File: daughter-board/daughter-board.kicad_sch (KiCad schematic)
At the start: 8 parts, among them J1 USB-C Connector, J2 Ribbon Connector, P1 IPOD_CONNECTOR_MALE, U1 AP2331SA-7

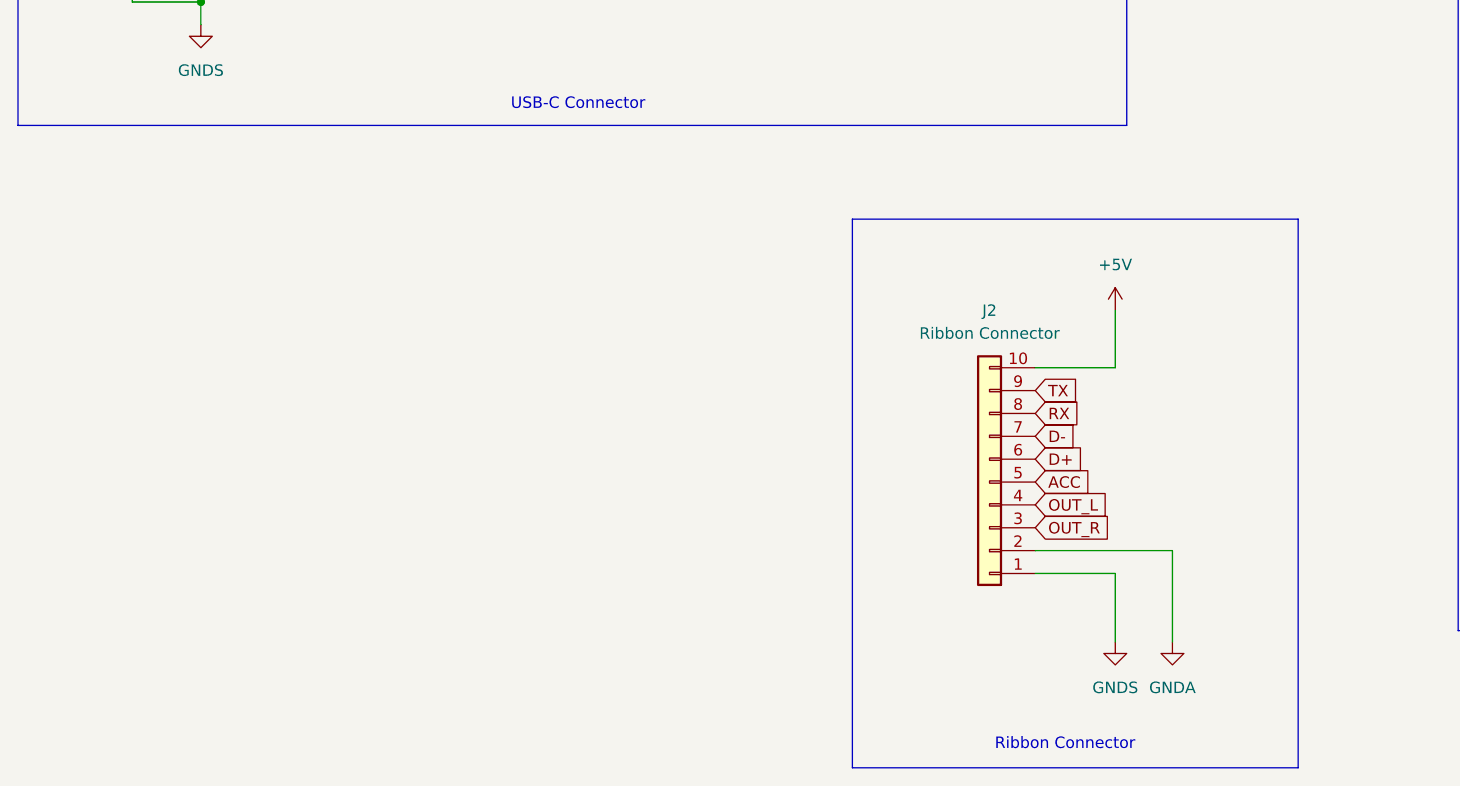
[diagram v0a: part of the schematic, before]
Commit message: Change FFC to match fab house.
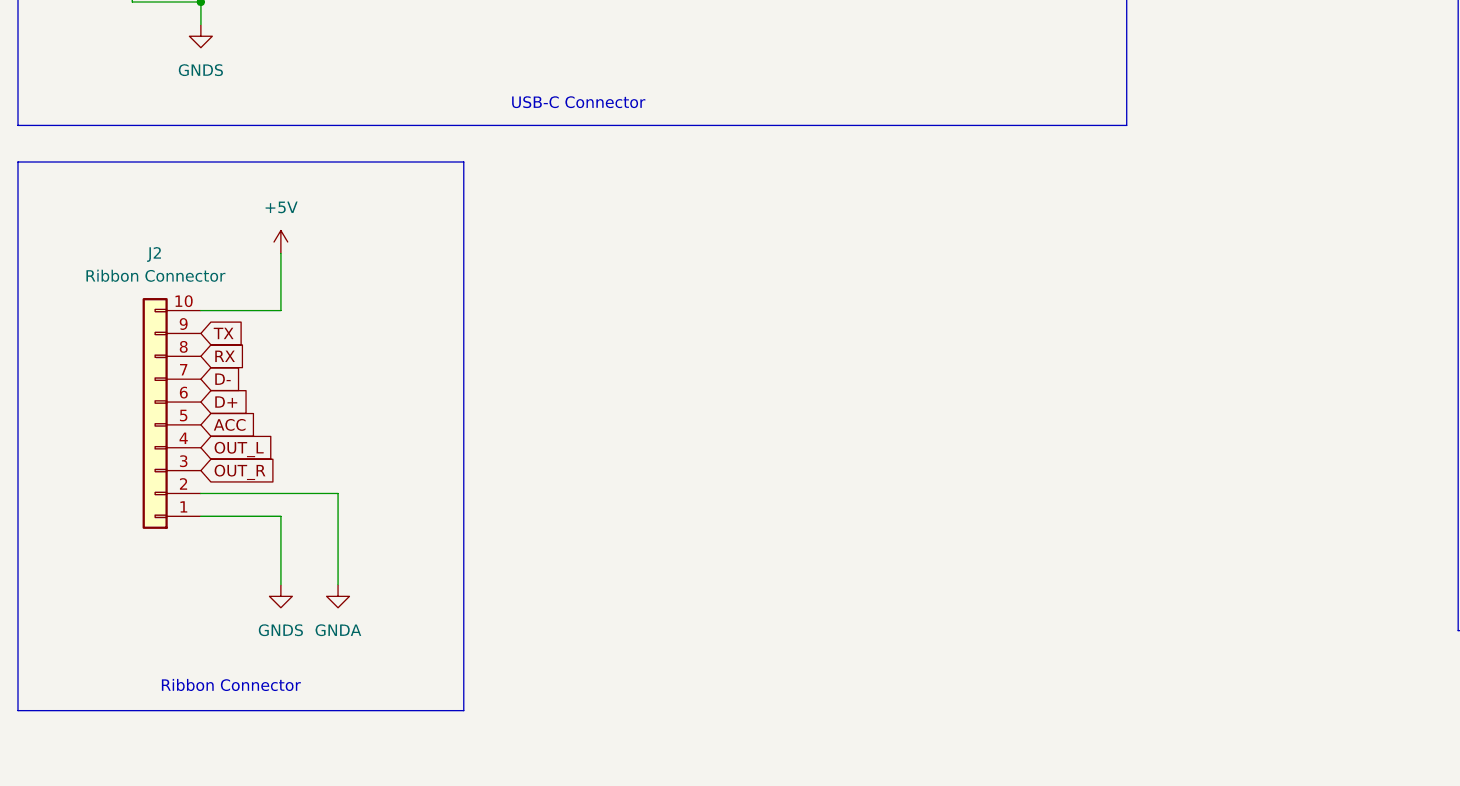
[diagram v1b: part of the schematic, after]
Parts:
- C1, C2: footprint (none) -> Capacitor_SMD:C_0805_2012Metric_Pad1.18x1.45mm_HandSolder
- J2: footprint (none) -> Connector_FFC-FPC:Molex_54548-1071_1x10-1MP_P0.5mm_Horizontal
- U1: footprint AP2331SA-7:SOT91P240X120-3N -> AP2331SA:SOT91P240X120-3N
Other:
- moved on the sheet: J2
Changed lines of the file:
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@@
 	(paper "A4")
 	(rectangle
-		(start 114.3 100.33)
-		(end 163.83 161.29)
+		(start 21.59 93.98)
+		(end 71.12 154.94)
 		(stroke
 			(width 0)
@@
 	(text "Ribbon Connector"
 		(exclude_from_sim no)
-		(at 137.922 158.75 0)
+		(at 45.212 152.4 0)
 		(effects
 			(font
@@
 	(wire
 		(pts
-			(xy 134.62 116.84) (xy 143.51 116.84)
-		)
-		(stroke
-			(width 0)
-			(type default)
-		)
-	)
-	(wire
-		(pts
-			(xy 143.51 139.7) (xy 143.51 147.32)
+			(xy 41.91 110.49) (xy 50.8 110.49)
+		)
+		(stroke
+			(width 0)
+			(type default)
+		)
+	)
+	(wire
+		(pts
+			(xy 50.8 133.35) (xy 50.8 140.97)
 		)
 		(stroke
@@
 	(wire
 		(pts
-			(xy 134.62 139.7) (xy 143.51 139.7)
+			(xy 41.91 133.35) (xy 50.8 133.35)
 		)
 		(stroke
@@
 	(wire
 		(pts
-			(xy 143.51 116.84) (xy 143.51 110.49)
+			(xy 50.8 110.49) (xy 50.8 104.14)
 		)
 		(stroke
@@
 	(wire
 		(pts
-			(xy 149.86 137.16) (xy 149.86 147.32)
+			(xy 57.15 130.81) (xy 57.15 140.97)
 		)
 		(stroke
@@
 	(wire
 		(pts
-			(xy 134.62 137.16) (xy 149.86 137.16)
+			(xy 41.91 130.81) (xy 57.15 130.81)
 		)
 		(stroke
@@
 	(global_label "ACC"
 		(shape input)
-		(at 134.62 129.54 0)
+		(at 41.91 123.19 0)
 		(fields_autoplaced yes)
 		(effects
@@
 		)
 		(property "Intersheetrefs" "${INTERSHEET_REFS}"
-			(at 141.2338 129.54 0)
+			(at 48.5238 123.19 0)
 			(effects
 				(font
@@
 	(global_label "D+"
 		(shape input)
-		(at 134.62 127 0)
+		(at 41.91 120.65 0)
 		(fields_autoplaced yes)
 		(effects
@@
 		)
 		(property "Intersheetrefs" "${INTERSHEET_REFS}"
-			(at 140.4476 127 0)
+			(at 47.7376 120.65 0)
 			(effects
 				(font
@@
 	(global_label "TX"
 		(shape input)
-		(at 134.62 119.38 0)
+		(at 41.91 113.03 0)
 		(fields_autoplaced yes)
 		(effects
@@
 		)
 		(property "Intersheetrefs" "${INTERSHEET_REFS}"
-			(at 139.7823 119.38 0)
+			(at 47.0723 113.03 0)
 			(effects
 				(font
@@
 	(global_label "D-"
 		(shape input)
-		(at 134.62 124.46 0)
+		(at 41.91 118.11 0)
 		(fields_autoplaced yes)
 		(effects
@@
 		)
 		(property "Intersheetrefs" "${INTERSHEET_REFS}"
-			(at 140.4476 124.46 0)
+			(at 47.7376 118.11 0)
 			(effects
 				(font
@@
 	(global_label "RX"
 		(shape input)
-		(at 134.62 121.92 0)
+		(at 41.91 115.57 0)
 		(fields_autoplaced yes)
 		(effects
@@
 		)
 		(property "Intersheetrefs" "${INTERSHEET_REFS}"
-			(at 140.0847 121.92 0)
+			(at 47.3747 115.57 0)
 			(effects
 				(font
@@
 	(global_label "OUT_L"
 		(shape input)
-		(at 134.62 132.08 0)
+		(at 41.91 125.73 0)
 		(fields_autoplaced yes)
 		(effects
@@
 		)
 		(property "Intersheetrefs" "${INTERSHEET_REFS}"
-			(at 143.2295 132.08 0)
+			(at 50.5195 125.73 0)
 			(effects
 				(font
@@
 	(global_label "OUT_R"
 		(shape input)
-		(at 134.62 134.62 0)
+		(at 41.91 128.27 0)
 		(fields_autoplaced yes)
 		(effects
@@
 		)
 		(property "Intersheetrefs" "${INTERSHEET_REFS}"
-			(at 143.4714 134.62 0)
+			(at 50.7614 128.27 0)
 			(effects
 				(font
@@
 			)
 		)
-		(property "Footprint" "AP2331SA-7:SOT91P240X120-3N"
+		(property "Footprint" "AP2331SA:SOT91P240X120-3N"
 			(at 107.95 38.1 0)
 			(effects
@@
 	(symbol
 		(lib_id "power:+5V")
-		(at 143.51 110.49 0)
+		(at 50.8 104.14 0)
 		(unit 1)
 		(exclude_from_sim no)
@@
 		(fields_autoplaced yes)
 		(property "Reference" "#PWR01"
-			(at 143.51 114.3 0)
+			(at 50.8 107.95 0)
 			(effects
 				(font
@@
 		)
 		(property "Value" "+5V"
-			(at 143.51 105.41 0)
+			(at 50.8 99.06 0)
 			(effects
 				(font
@@
 		)
 		(property "Footprint" ""
-			(at 143.51 110.49 0)
+			(at 50.8 104.14 0)
 			(effects
 				(font
@@
 		)
 		(property "Datasheet" ""
-			(at 143.51 110.49 0)
+			(at 50.8 104.14 0)
 			(effects
 				(font
@@
 		)
 		(property "Description" "Power symbol creates a global label with name \"+5V\""
-			(at 143.51 110.49 0)
+			(at 50.8 104.14 0)
 			(effects
 				(font
@@
 	(symbol
 		(lib_id "power:GNDA")
-		(at 149.86 147.32 0)
+		(at 57.15 140.97 0)
 		(unit 1)
 		(exclude_from_sim no)
@@
 		(fields_autoplaced yes)
 		(property "Reference" "#PWR011"
-			(at 149.86 153.67 0)
+			(at 57.15 147.32 0)
 			(effects
 				(font
@@
 		)
 		(property "Value" "GNDA"
-			(at 149.86 152.4 0)
+			(at 57.15 146.05 0)
 			(effects
 				(font
@@
 		)
 		(property "Footprint" ""
-			(at 149.86 147.32 0)
+			(at 57.15 140.97 0)
 			(effects
 				(font
@@
 		)
 		(property "Datasheet" ""
-			(at 149.86 147.32 0)
+			(at 57.15 140.97 0)
 			(effects
 				(font
@@
 		)
 		(property "Description" "Power symbol creates a global label with name \"GNDA\" , analog ground"
-			(at 149.86 147.32 0)
+			(at 57.15 140.97 0)
 			(effects
 				(font
@@
 			)
 		)
-		(property "Footprint" ""
+		(property "Footprint" "Capacitor_SMD:C_0805_2012Metric_Pad1.18x1.45mm_HandSolder"
 			(at 129.2352 43.18 0)
 			(effects
@@
 	(symbol
 		(lib_id "Connector_Generic:Conn_01x10")
-		(at 129.54 129.54 180)
+		(at 36.83 123.19 180)
 		(unit 1)
 		(exclude_from_sim no)
@@
 		(fields_autoplaced yes)
 		(property "Reference" "J2"
-			(at 129.54 110.49 0)
+			(at 36.83 104.14 0)
 			(effects
 				(font
@@
 		)
 		(property "Value" "Ribbon Connector"
-			(at 129.54 113.03 0)
-			(effects
-				(font
-					(size 1.27 1.27)
-				)
-			)
-		)
-		(property "Footprint" ""
-			(at 129.54 129.54 0)
+			(at 36.83 106.68 0)
+			(effects
+				(font
+					(size 1.27 1.27)
+				)
+			)
+		)
+		(property "Footprint" "Connector_FFC-FPC:Molex_54548-1071_1x10-1MP_P0.5mm_Horizontal"
+			(at 36.83 123.19 0)
 			(effects
 				(font
@@
 		)
 		(property "Datasheet" "~"
-			(at 129.54 129.54 0)
+			(at 36.83 123.19 0)
 			(effects
 				(font
@@
 		)
 		(property "Description" "Generic connector, single row, 01x10, script generated (kicad-library-utils/schlib/autogen/connector/)"
-			(at 129.54 129.54 0)
+			(at 36.83 123.19 0)
 			(effects
 				(font
@@
 	(symbol
 		(lib_id "power:GNDS")
-		(at 143.51 147.32 0)
+		(at 50.8 140.97 0)
 		(unit 1)
 		(exclude_from_sim no)
@@
 		(fields_autoplaced yes)
 		(property "Reference" "#PWR05"
-			(at 143.51 153.67 0)
+			(at 50.8 147.32 0)
 			(effects
 				(font
@@
 		)
 		(property "Value" "GNDS"
-			(at 143.51 152.4 0)
+			(at 50.8 146.05 0)
 			(effects
 				(font
@@
 		)
 		(property "Footprint" ""
-			(at 143.51 147.32 0)
+			(at 50.8 140.97 0)
 			(effects
 				(font
@@
 		)
 		(property "Datasheet" ""
-			(at 143.51 147.32 0)
+			(at 50.8 140.97 0)
 			(effects
 				(font
@@
 		)
 		(property "Description" "Power symbol creates a global label with name \"GNDS\" , signal ground"
-			(at 143.51 147.32 0)
+			(at 50.8 140.97 0)
 			(effects
 				(font
@@
 			)
 		)
-		(property "Footprint" ""
+		(property "Footprint" "Capacitor_SMD:C_0805_2012Metric_Pad1.18x1.45mm_HandSolder"
 			(at 89.8652 43.18 0)
 			(effects

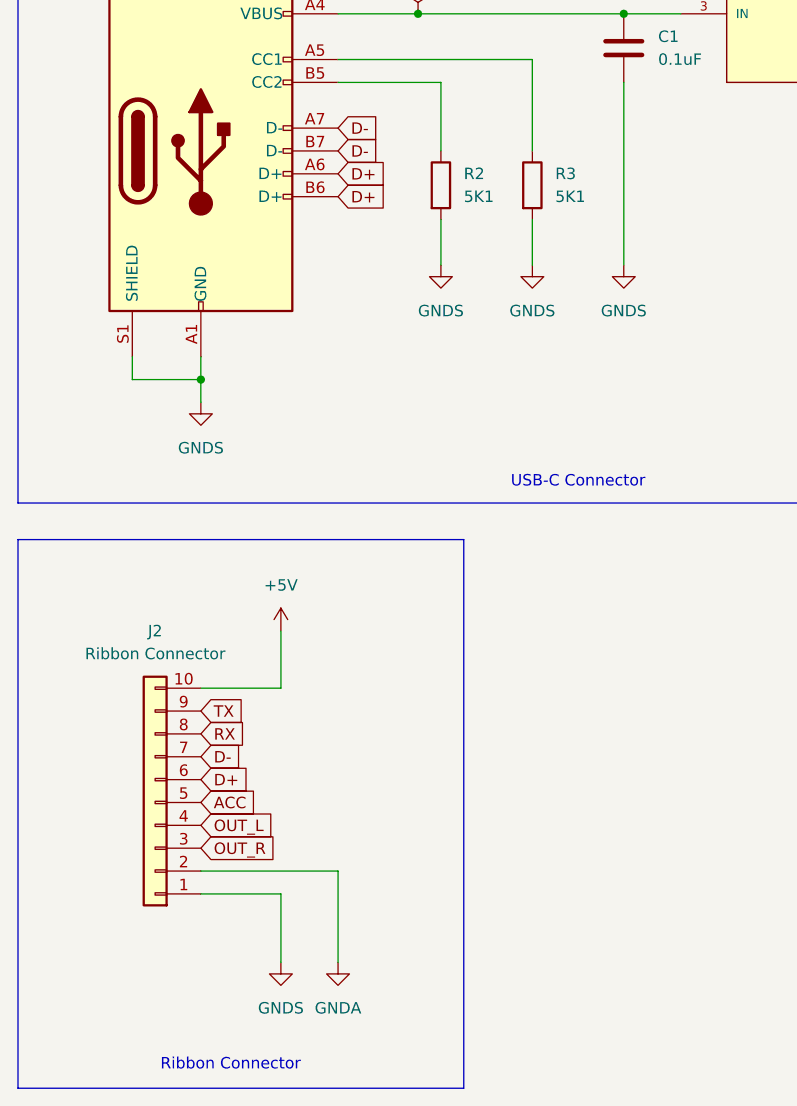
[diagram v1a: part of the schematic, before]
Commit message: FFC routing
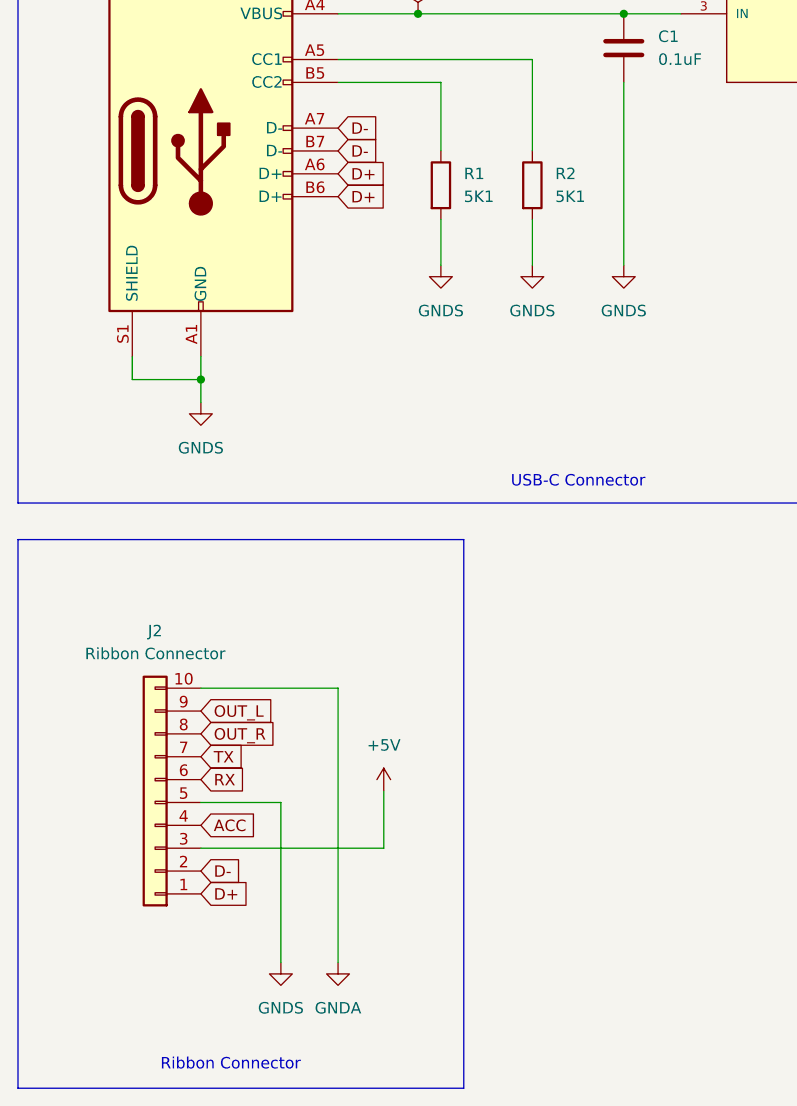
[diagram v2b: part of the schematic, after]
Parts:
- renumbered R2 to R1, R3 to R2
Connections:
- net +5V: now also J2.3 (Pin_3); no longer J2.10 (Pin_10)
- net ACC: now also J2.4 (Pin_4); no longer J2.5 (Pin_5)
- net D+: now also J2.1 (Pin_1); no longer J2.6 (Pin_6)
- net D-: now also J2.2 (Pin_2); no longer J2.7 (Pin_7)
- net GNDA: now also J2.10 (Pin_10); no longer J2.2 (Pin_2)
- net GNDS: now also J2.5 (Pin_5); no longer J2.1 (Pin_1)
- net OUT_L: now also J2.9 (Pin_9); no longer J2.4 (Pin_4)
- net OUT_R: now also J2.8 (Pin_8); no longer J2.3 (Pin_3)
- net RX: now also J2.6 (Pin_6); no longer J2.8 (Pin_8)
- net TX: now also J2.7 (Pin_7); no longer J2.9 (Pin_9)

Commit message: Eh, not sure about this.
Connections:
- net +5V: now also J2.8 (Pin_8); no longer J2.3 (Pin_3)
- net ACC: now also J2.7 (Pin_7); no longer J2.4 (Pin_4)
- net D+: now also J2.10 (Pin_10); no longer J2.1 (Pin_1)
- net D-: now also J2.9 (Pin_9); no longer J2.2 (Pin_2)
- net GNDA: now also J2.1 (Pin_1); no longer J2.10 (Pin_10)
- net GNDS: now also J2.6 (Pin_6); no longer J2.5 (Pin_5)
- net OUT_L: now also J2.3 (Pin_3); no longer J2.9 (Pin_9)
- net OUT_R: now also J2.2 (Pin_2); no longer J2.8 (Pin_8)
- net RX: now also J2.5 (Pin_5); no longer J2.6 (Pin_6)
- net TX: now also J2.4 (Pin_4); no longer J2.7 (Pin_7)
